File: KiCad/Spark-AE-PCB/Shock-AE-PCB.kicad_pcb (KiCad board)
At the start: 2 copper layers, 50 x 100 mm, 21 parts, among them J1 SSM-120-L-SV-BE, J2 SSM-120-L-SV-BE, J3 Conn_02x10_Odd_Even, J4 Conn_02x05_Odd_Even, J5 Conn_01x08_Socket, J6 Conn_01x08_Socket, J7 UJ32-C-V-G-TH-5-P24-TR, SW1 SW_Push, SW2 SW_Push, U1 PJS008U-3000-0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

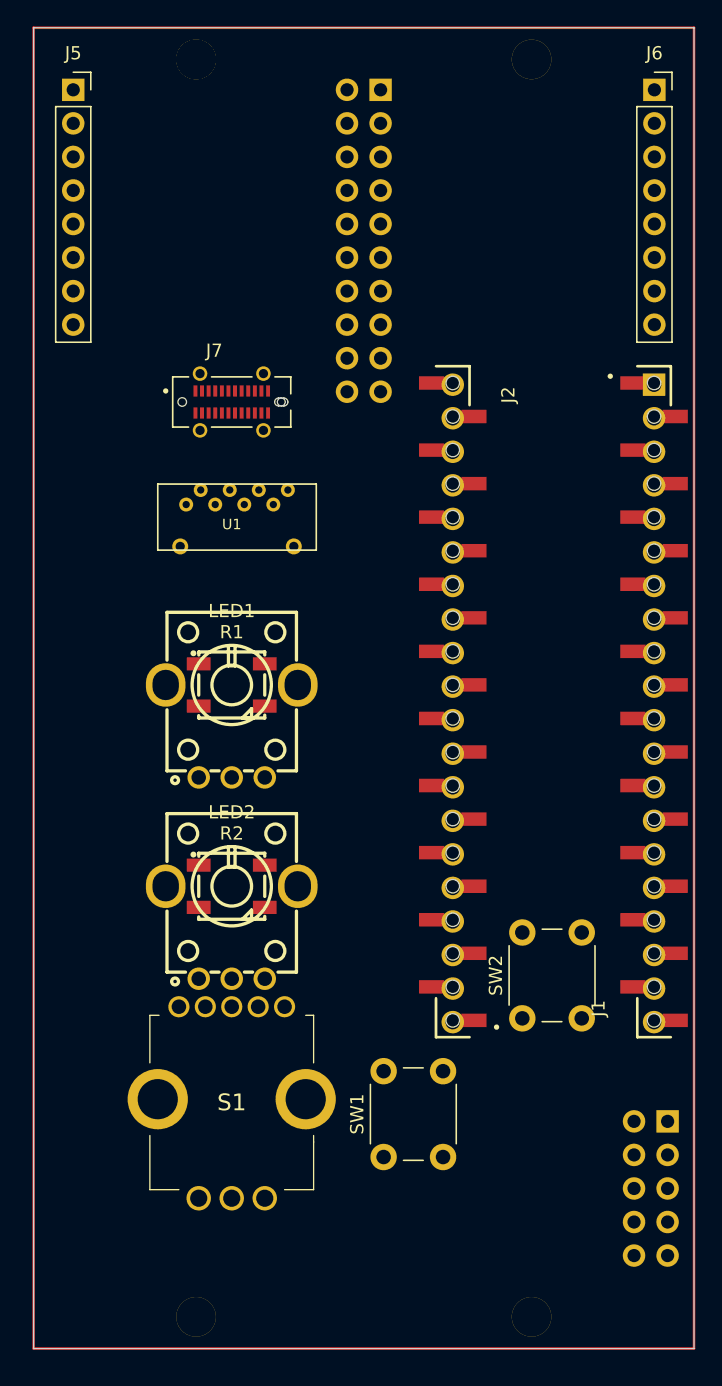
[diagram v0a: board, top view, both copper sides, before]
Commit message: rearranged Shock controls to be aligned and offset with bus connector
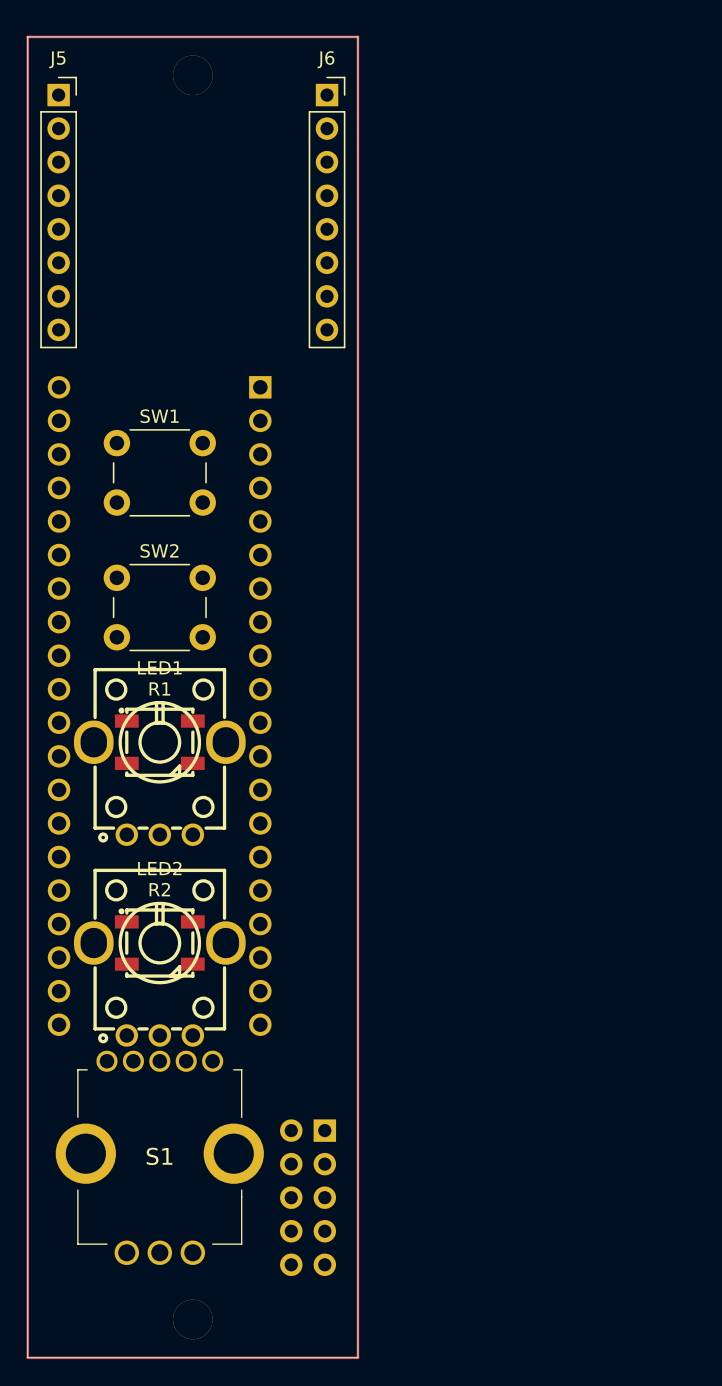
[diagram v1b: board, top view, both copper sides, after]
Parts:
- removed the ? at (107.9, 51.4)
- removed the ? at (133.3, 146.6)
- removed the ? at (133.3, 51.4)
- removed J1, J2: SSM-120-L-SV-BE, clectric-diy:SAMTEC_SSM-120-L-SV-BE
- removed J3: Conn_02x10_Odd_Even, Connector_PinHeader_2.54mm:PinHeader_2x10_P2.54mm_Vertical
- removed J7: UJ32-C-V-G-TH-5-P24-TR, clectric-diy:SAMESKY_UJ32-C-V-G-TH-5-P24-TR
- removed U1: PJS008U-3000-0, clectric-diy:PJS008U-3000-0
- moved SW1 57.7 mm to (101.9, 80.5), turned to 0 degrees
- moved SW2 45.3 mm to (101.9, 90.7), turned to 0 degrees
- moved U2 29.8 mm to (112.7, 76.3)
- moved J4 26.0 mm to (117.6, 132.5)
- moved J6 24.8 mm to (117.8, 54.1)
- moved LED1 6.96 mm to (105.1, 103.1)
- moved R1 6.96 mm to (105.1, 106.6)
- moved LED2 6.94 mm to (105.1, 118.3)
- moved R2 6.94 mm to (105.1, 121.8)
- moved S1 6.83 mm to (105.1, 134.5)
- moved ? 1.22 mm to (107.6, 52.6)
- moved J5 1.17 mm to (97.5, 54.1)
- moved ? 0.32 mm to (107.6, 146.8)
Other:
- board size 50 x 100 mm -> 25 x 100 mm
